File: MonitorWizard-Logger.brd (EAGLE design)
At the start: 84.4 x 80 mm, 40 parts, among them CON1 MICROSD, IC1 LD117AV33, J1 22-27-2041-04, J2 22-27-2041-04, J3 22-27-2041-04, U1 DHT22, U2 RFM69HW, U3 LTC3531, U4-NRF24L01 NRF24L01+-PCB-AERIAL, U6 ATMEGA328P-PU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

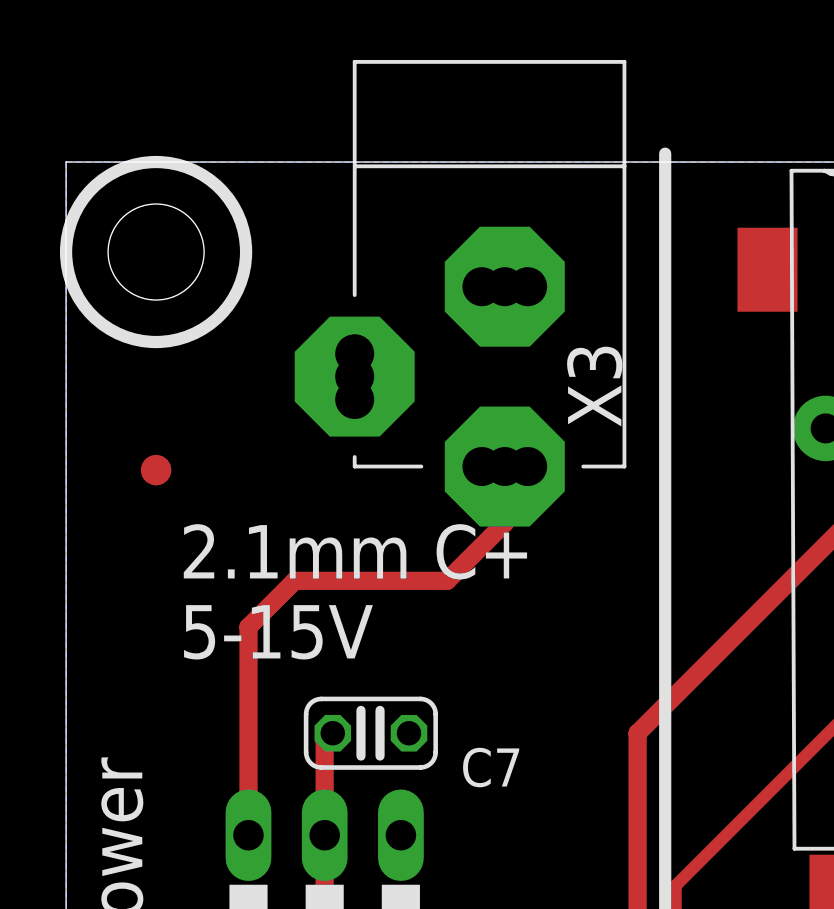
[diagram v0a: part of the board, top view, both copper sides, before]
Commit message: Change to a better barrel jack footprint
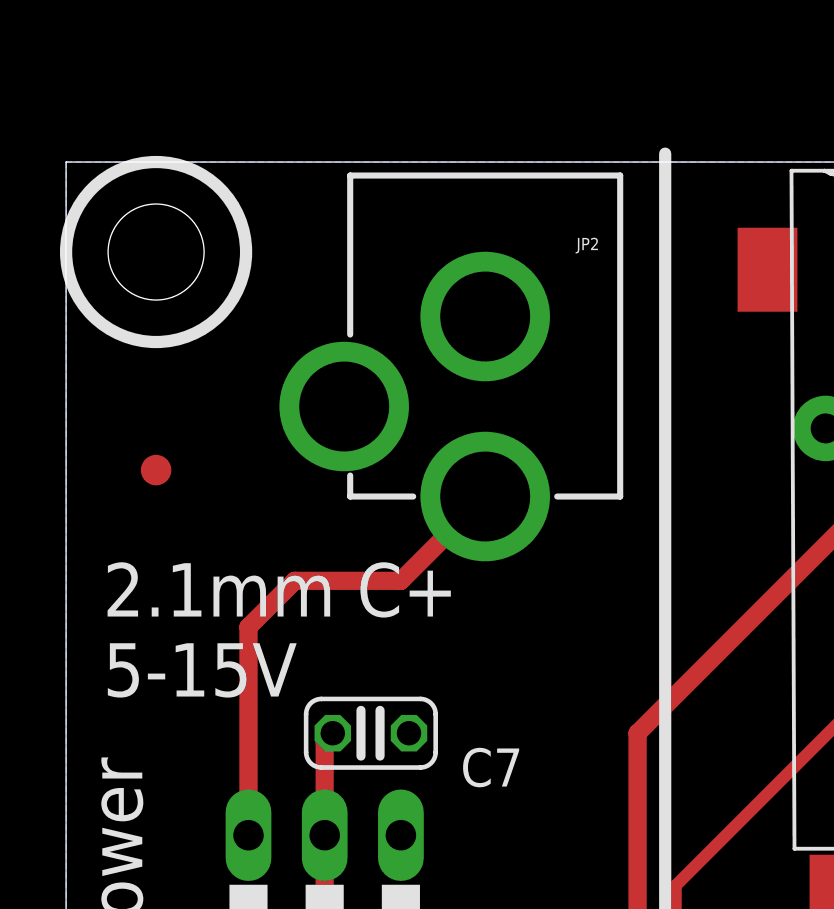
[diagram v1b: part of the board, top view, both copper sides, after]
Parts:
- removed X3: POWERSUPPLY_DC21MMX, SmartPrj:POWERSUPPLY_DC-21MM
- added JP2: POWER_JACKPTH, SparkFun-Connectors:POWER_JACK_PTH
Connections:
- net GND: now also JP2.GND, JP2.GNDBREAK; no longer X3.1, X3.3
- net VBJ: now also JP2.PWR; no longer X3.2
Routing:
- net VBJ: track 18.8 -> 16.6 mm
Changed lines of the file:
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@@
 <text x="33.94" y="2.54" size="1.778" layer="21" font="vector">MonitorWizard Development Board V1</text>
 <text x="32.67" y="36.83" size="1.778" layer="21" font="vector">Sensing</text>
-<text x="15.1925" y="63.4525" size="1.778" layer="21" font="vector">2.1mm C+
+<text x="12.6525" y="62.1825" size="1.778" layer="21" font="vector">2.1mm C+
 5-15V</text>
 <text x="66.23" y="76.2" size="1.778" layer="21" font="vector">Wireless</text>
@@
 </element>
 <element name="GND" library="Probes" package="ALLIGATOR" value="ALLIGATOR" x="22.94" y="0"/>
-<element name="X3" library="SmartPrj" package="POWERSUPPLY_DC-21MM" value="POWERSUPPLY_DC21MMX" x="26.13" y="76.2" smashed="yes">
-<attribute name="NAME" x="29.94" y="71.12" size="1.778" layer="25" ratio="5" rot="R90"/>
-</element>
 <element name="FD4" library="SmartPrj" package="FIDUCIA-MOUNT" value="FIDUCIALMOUNT" x="92.79" y="10.27"/>
 <element name="I_SENSE" library="Probes" package="CURRENT_MEASURE" value="CURRENT_MEASURE_0.4A" x="29.16" y="11.25" smashed="yes" rot="R180">
@@
 </element>
 <element name="C8" library="rcl" package="E2,5-6" value="" x="23.8125" y="34.6075" rot="R180"/>
+<element name="JP2" library="SparkFun-Connectors" package="POWER_JACK_PTH" value="POWER_JACKPTH" x="25.4" y="82.55" rot="R180">
+<attribute name="PROD_ID" value="CONN-08197" x="25.4" y="82.55" size="1.778" layer="27" rot="R180" display="off"/>
+</element>
 </elements>
 <signals>
@@
 <contactref element="GND" pad="TOP"/>
 <contactref element="GND" pad="BTM"/>
-<contactref element="X3" pad="3"/>
-<contactref element="X3" pad="1"/>
 <contactref element="U4-NRF24L01" pad="P$1"/>
 <contactref element="U6" pad="8"/>
@@
 <wire x1="22.94" y1="3.4925" x2="23.82" y2="3.5" width="0.6096" layer="16"/>
 <wire x1="23.82" y1="3.5" x2="22.94" y2="3.5" width="0.6096" layer="16"/>
+<contactref element="JP2" pad="GNDBREAK"/>
+<contactref element="JP2" pad="GND"/>
 </signal>
 <signal name="AREF" class="4">
@@
 </signal>
 <signal name="VBJ">
-<contactref element="X3" pad="2"/>
 <contactref element="IC1" pad="3"/>
 <wire x1="17.51" y1="57.56" x2="17.51" y2="64.5" width="0.6096" layer="1"/>
 <wire x1="17.51" y1="64.5" x2="19.05" y2="66.04" width="0.6096" layer="1"/>
-<wire x1="19.05" y1="66.04" x2="24.13" y2="66.04" width="0.6096" layer="1"/>
-<wire x1="24.13" y1="66.04" x2="26.0538" y2="67.9638" width="0.6096" layer="1"/>
-<wire x1="26.0538" y1="67.9638" x2="26.0538" y2="69.85" width="0.6096" layer="1"/>
+<contactref element="JP2" pad="PWR"/>
+<wire x1="19.05" y1="66.04" x2="22.59" y2="66.04" width="0.6096" layer="1"/>
+<wire x1="22.59" y1="66.04" x2="25.4" y2="68.85" width="0.6096" layer="1"/>
 </signal>
 <signal name="DHT22_DATA">

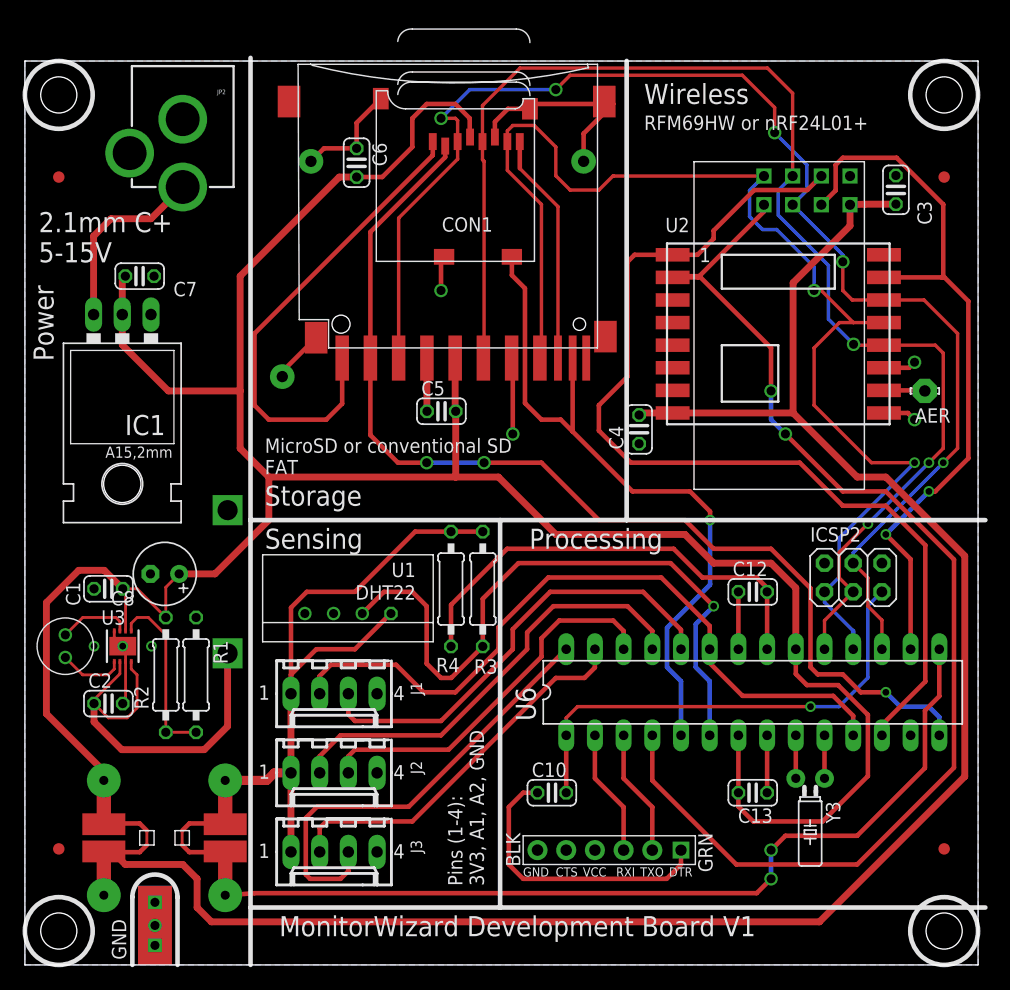
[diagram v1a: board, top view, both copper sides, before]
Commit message: Change footprint for LTC3531
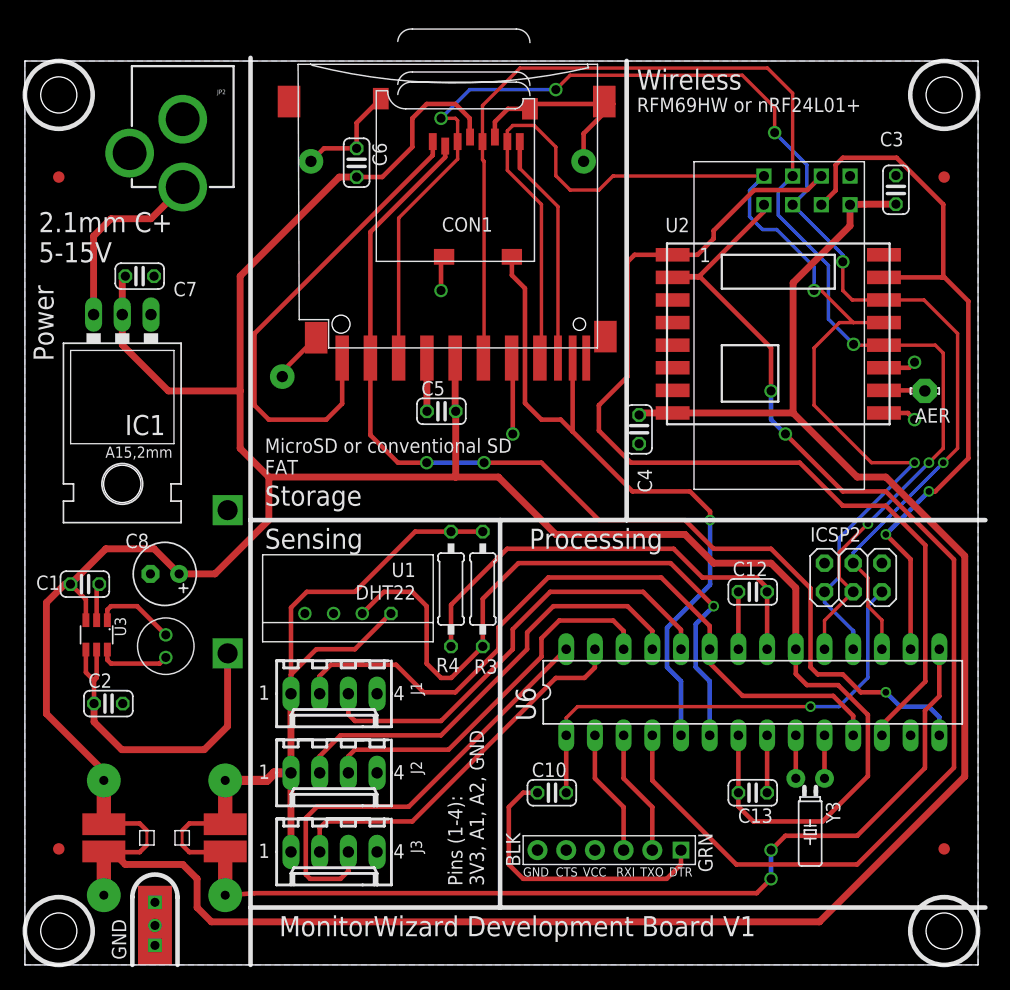
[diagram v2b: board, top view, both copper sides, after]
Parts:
- removed R1, R2: (no value), resistor:0207/10
- U3: device exported-lbrlinear-sen:DFN8-3X3 -> custom:TSOT23-6
- moved L1 8.89 mm to (23.9, 28.2)
- moved U3 2.52 mm to (17.8, 29.2), turned to 180 degrees
- moved C1 2.12 mm to (16.7, 33.7), turned to 0 degrees
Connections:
- removed net N$3: R1.2, R2.1, U3.5
- net 3V3: now also U3.3; no longer R2.2, U3.6
- net GND: now also U3.2; no longer R1.1, U3.3, U3.8, U3.EXP
- net N$1: now also U3.1; no longer U3.7
- net N$2: now also U3.6; no longer U3.1
- net VBAT: now also U3.5; no longer U3.2
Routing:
- net N$3: track 15.9 -> 0.00 mm
- net VBAT: track 35.6 -> 29.7 mm
- net GND: track 74.3 -> 70.5 mm, vias 11 -> 8
- net 3V3: track 222.7 -> 219.6 mm
- net N$1: track 6.45 -> 7.27 mm
- net N$2: track 5.85 -> 6.45 mm

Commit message: Move some stuff around, add a filter capacitor. As ordered from Screenbond
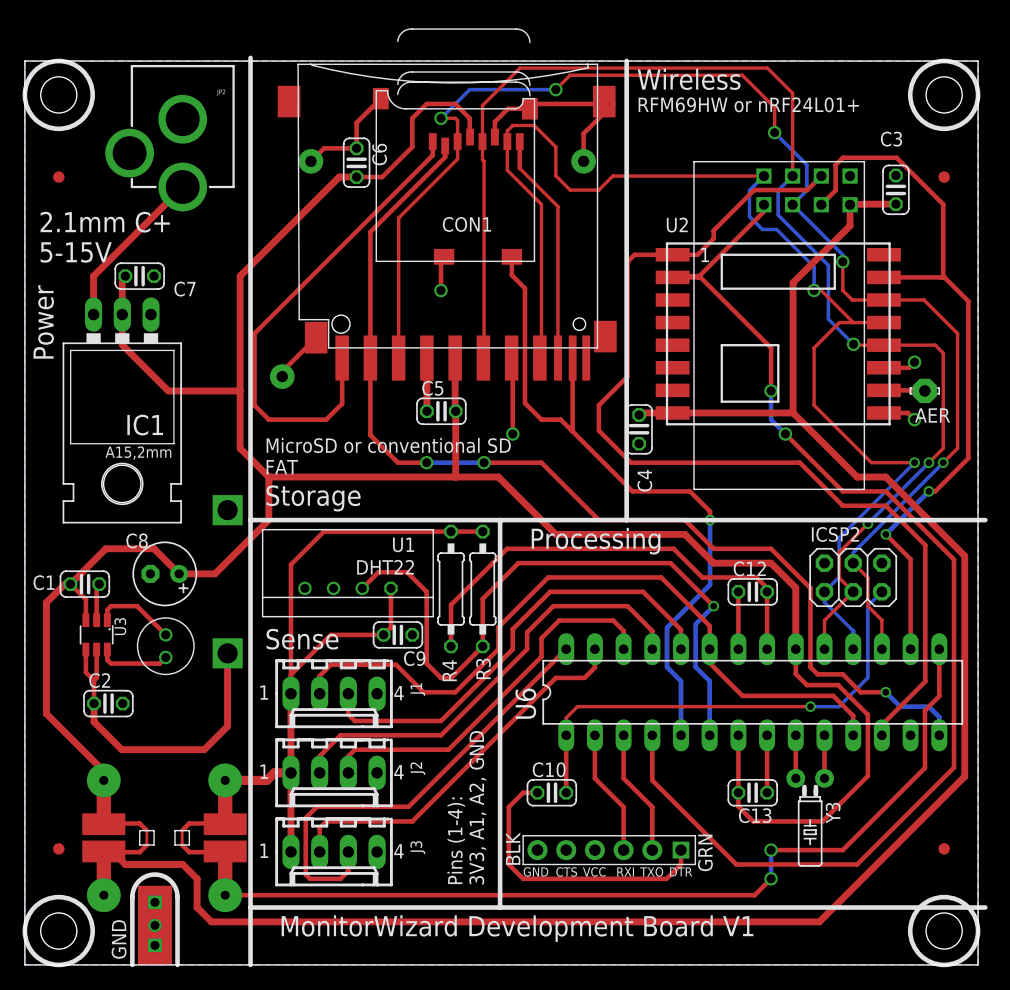
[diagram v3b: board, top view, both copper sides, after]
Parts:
- added C9: 0.1u, rcl:C025-024X044
- moved U1 2.22 mm to (40.0, 33.3)
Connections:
- net GND: now also C9.1
- net SENSOR_3V3: now also C9.2
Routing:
- net SENSOR_3V3: track 60.3 -> 65.4 mm
- net VBJ: track 16.6 -> 14.6 mm
- net DHT22_DATA: track 58.9 -> 60.1 mm
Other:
- board text added: "Sense"
- board text removed: "Sensing"
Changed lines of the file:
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@@
 <wire x1="11.43" y1="80" x2="11.43" y2="0" width="0" layer="20"/>
 <text x="33.94" y="2.54" size="1.778" layer="21" font="vector">MonitorWizard Development Board V1</text>
-<text x="32.67" y="36.83" size="1.778" layer="21" font="vector">Sensing</text>
+<text x="32.67" y="27.94" size="1.778" layer="21" font="vector">Sense</text>
 <text x="12.6525" y="62.1825" size="1.778" layer="21" font="vector">2.1mm C+
 5-15V</text>
@@
 <attribute name="NAME" x="26.085" y="12.795" size="0.8128" layer="27" rot="R90"/>
 </element>
-<element name="U1" library="RHT03_DHT-22_AM2302" package="RHT03_DHT-22" value="DHT22" x="40.02" y="31.1" rot="R180">
-<attribute name="PROD_ID" value="SEN-10167" x="40.02" y="31.1" size="1.778" layer="27" rot="R180" display="off"/>
+<element name="U1" library="RHT03_DHT-22_AM2302" package="RHT03_DHT-22" value="DHT22" x="40.02" y="33.3225" rot="R180">
+<attribute name="PROD_ID" value="SEN-10167" x="40.02" y="33.3225" size="1.778" layer="27" rot="R180" display="off"/>
 </element>
 <element name="R3" library="resistor" package="0207/10" value="10K" x="51.955" y="33.27" smashed="yes" rot="R90">
-<attribute name="NAME" x="51.177" y="25.769" size="1.27" layer="25" ratio="10"/>
+<attribute name="NAME" x="52.6535" y="25.142" size="1.27" layer="25" ratio="10" rot="R90"/>
 <attribute name="VALUE" x="51.2325" y="35.6656" size="1.27" layer="27" ratio="10" rot="R270"/>
 </element>
@@
 <element name="L1" library="InductorsThru" package="L-RADIAL-2-5OD" value="10uH" x="23.9" y="28.21" smashed="yes" rot="R90"/>
 <element name="C1" library="rcl" package="C025-024X044" value="10uH" x="16.74" y="33.7025" smashed="yes">
-<attribute name="NAME" x="12.422" y="33.1945" size="1.27" layer="25" ratio="10"/>
-<attribute name="VALUE" x="13.057" y="35.163" size="1.27" layer="27" ratio="10"/>
+<attribute name="NAME" x="12.1045" y="33.1945" size="1.27" layer="25" ratio="10"/>
+<attribute name="VALUE" x="12.1045" y="35.163" size="1.27" layer="27" ratio="10"/>
 </element>
 <element name="C2" library="rcl" package="C025-024X044" value="2.2uH" x="18.82" y="23.13"/>
@@
 </element>
 <element name="R4" library="resistor" package="0207/10" value="TBD" x="49.145" y="33.27" smashed="yes" rot="R270">
-<attribute name="NAME" x="47.8195" y="25.904" size="1.27" layer="25" ratio="10"/>
+<attribute name="NAME" x="49.661" y="24.9595" size="1.27" layer="25" ratio="10" rot="R90"/>
 <attribute name="VALUE" x="48.51" y="35.5306" size="1.27" layer="27" ratio="10" rot="R270"/>
 </element>
@@
 <attribute name="VALUE" x="14.9225" y="30.7975" size="1.016" layer="27" ratio="10" rot="R270"/>
 <attribute name="NAME" x="19.3675" y="30.7975" size="1.016" layer="25" ratio="10" rot="R270"/>
+</element>
+<element name="C9" library="rcl" package="C025-024X044" value="0.1u" x="44.45" y="29.21" smashed="yes" rot="R180">
+<attribute name="NAME" x="44.8945" y="26.4795" size="1.27" layer="25" ratio="10"/>
 </element>
 </elements>
@@
 <contactref element="C2" pad="2"/>
 <contactref element="C1" pad="2"/>
-<wire x1="20.34" y1="23.13" x2="20.09" y2="23.13" width="0" layer="19" extent="1-16"/>
 <contactref element="IC1" pad="1"/>
 <wire x1="77.12" y1="15.24" x2="77.12" y2="20.32" width="0.4064" layer="1"/>
@@
 <wire x1="17.78" y1="33.4725" x2="17.78" y2="30.51" width="0.4064" layer="1"/>
 <wire x1="17.78" y1="33.4725" x2="18.01" y2="33.7025" width="0.4064" layer="1"/>
+<contactref element="C9" pad="1"/>
 </signal>
 <signal name="AREF" class="4">
@@
 <signal name="VBJ">
 <contactref element="IC1" pad="3"/>
-<wire x1="17.51" y1="57.56" x2="17.51" y2="64.5" width="0.6096" layer="1"/>
-<wire x1="17.51" y1="64.5" x2="19.05" y2="66.04" width="0.6096" layer="1"/>
+<wire x1="17.51" y1="57.56" x2="17.51" y2="60.96" width="0.6096" layer="1"/>
+<wire x1="17.51" y1="60.96" x2="22.59" y2="66.04" width="0.6096" layer="1"/>
 <contactref element="JP2" pad="PWR"/>
-<wire x1="19.05" y1="66.04" x2="22.59" y2="66.04" width="0.6096" layer="1"/>
 <wire x1="22.59" y1="66.04" x2="25.4" y2="68.85" width="0.6096" layer="1"/>
 </signal>
@@
 <wire x1="55.11" y1="35.56" x2="51.955" y2="32.405" width="0.4064" layer="1"/>
 <wire x1="51.955" y1="32.405" x2="51.955" y2="28.19" width="0.4064" layer="1"/>
-<wire x1="41.29" y1="31.1" x2="43.21" y2="33.02" width="0.4064" layer="1"/>
-<wire x1="43.21" y1="33.02" x2="45.72" y2="33.02" width="0.4064" layer="1"/>
-<wire x1="45.72" y1="33.02" x2="46.99" y2="31.75" width="0.4064" layer="1"/>
-<wire x1="46.99" y1="31.75" x2="46.99" y2="26.67" width="0.4064" layer="1"/>
+<wire x1="41.29" y1="33.3225" x2="42.72186875" y2="34.75436875" width="0.4064" layer="1"/>
+<wire x1="42.72186875" y1="34.75436875" x2="45.25563125" y2="34.75436875" width="0.4064" layer="1"/>
+<wire x1="45.25563125" y1="34.75436875" x2="46.99" y2="33.02" width="0.4064" layer="1"/>
+<wire x1="46.99" y1="33.02" x2="46.99" y2="26.67" width="0.4064" layer="1"/>
 <wire x1="46.99" y1="26.67" x2="48.26" y2="25.4" width="0.4064" layer="1"/>
 <wire x1="48.26" y1="25.4" x2="49.165" y2="25.4" width="0.4064" layer="1"/>
@@
 <wire x1="20.32" y1="60.96" x2="20.05" y2="60.69" width="0.6096" layer="1"/>
 <wire x1="20.05" y1="60.69" x2="20.05" y2="57.56" width="0.6096" layer="1"/>
-<wire x1="23.9" y1="33.425" x2="25.0825" y2="34.6075" width="0" layer="19" extent="1-16"/>
 <wire x1="25.0825" y1="34.6075" x2="28.2575" y2="34.6075" width="0.6096" layer="1"/>
 <wire x1="28.2575" y1="34.6075" x2="33.02" y2="39.37" width="0.6096" layer="1"/>
@@
 <wire x1="92.36" y1="23.78" x2="91.09" y2="22.51" width="0.4064" layer="1"/>
 <wire x1="91.09" y1="22.51" x2="91.09" y2="17.43" width="0.4064" layer="1"/>
-<wire x1="91.09" y1="17.43" x2="85.09" y2="11.43" width="0.4064" layer="1"/>
-<wire x1="85.09" y1="11.43" x2="78.74" y2="11.43" width="0.4064" layer="1"/>
-<wire x1="78.74" y1="11.43" x2="77.47" y2="10.16" width="0.4064" layer="1"/>
-<via x="77.47" y="10.16" extent="1-16" drill="0.8" shape="square"/>
+<wire x1="91.09" y1="17.43" x2="83.82" y2="10.16" width="0.4064" layer="1"/>
+<via x="77.47" y="10.16" extent="1-16" drill="0.8"/>
 <wire x1="77.47" y1="10.16" x2="77.47" y2="7.62" width="0.4064" layer="16"/>
-<via x="77.47" y="7.62" extent="1-16" drill="0.8" shape="square"/>
-<wire x1="77.47" y1="7.62" x2="76.2" y2="6.35" width="0.4064" layer="1"/>
-<wire x1="76.2" y1="6.35" x2="31.75" y2="6.35" width="0.4064" layer="1"/>
-<wire x1="31.75" y1="6.35" x2="29.39" y2="6.17" width="0.4064" layer="1"/>
-<wire x1="29.39" y1="6.17" x2="29.16" y2="6.17" width="0.4064" layer="1"/>
+<via x="77.47" y="7.62" extent="1-16" drill="0.8"/>
+<wire x1="77.47" y1="7.62" x2="76.02" y2="6.17" width="0.4064" layer="1"/>
+<wire x1="29.16" y1="6.17" x2="76.02" y2="6.17" width="0.4064" layer="1"/>
+<wire x1="77.47" y1="10.16" x2="83.82" y2="10.16" width="0.4064" layer="1"/>
 </signal>
 <signal name="N$1">
@@
 <contactref element="R4" pad="1"/>
 <wire x1="34.98" y1="24" x2="34.98" y2="17" width="0.6096" layer="1"/>
-<wire x1="43.83" y1="31.1" x2="43.8" y2="31.1" width="0.4064" layer="1"/>
-<wire x1="43.8" y1="31.1" x2="40.64" y2="27.94" width="0.4064" layer="1"/>
-<wire x1="40.64" y1="27.94" x2="37.22396875" y2="27.94" width="0.4064" layer="1"/>
-<wire x1="37.22396875" y1="27.94" x2="34.98" y2="25.69603125" width="0.4064" layer="1"/>
+<wire x1="38.49396875" y1="29.21" x2="34.98" y2="25.69603125" width="0.4064" layer="1"/>
 <wire x1="34.98" y1="25.69603125" x2="34.98" y2="24" width="0.4064" layer="1"/>
 <wire x1="34.98" y1="17" x2="34.98" y2="10" width="0.6096" layer="1"/>
 <wire x1="33.51" y1="17" x2="34.98" y2="17" width="0.8128" layer="1"/>
 <wire x1="51.955" y1="38.35" x2="49.145" y2="38.35" width="0.4064" layer="1"/>
-<wire x1="49.145" y1="38.35" x2="45.97" y2="38.35" width="0.4064" layer="1"/>
-<wire x1="45.97" y1="38.35" x2="40.64" y2="33.02" width="0.4064" layer="1"/>
-<wire x1="40.64" y1="33.02" x2="36.376171875" y2="33.02" width="0.4064" layer="1"/>
-<wire x1="36.376171875" y1="33.02" x2="34.98" y2="31.623828125" width="0.4064" layer="1"/>
-<wire x1="34.98" y1="31.623828125" x2="34.98" y2="24" width="0.4064" layer="1"/>
+<wire x1="49.145" y1="38.35" x2="37.896171875" y2="38.35" width="0.4064" layer="1"/>
+<wire x1="37.896171875" y1="38.35" x2="34.98" y2="35.433828125" width="0.4064" layer="1"/>
+<wire x1="34.98" y1="35.433828125" x2="34.98" y2="24" width="0.4064" layer="1"/>
 <wire x1="33.51" y1="17" x2="32.84" y2="16.33" width="0.8128" layer="1"/>
 <wire x1="32.84" y1="16.33" x2="29.16" y2="16.33" width="0.8128" layer="1"/>
+<contactref element="C9" pad="2"/>
+<wire x1="38.49396875" y1="29.21" x2="43.18" y2="29.21" width="0.4064" layer="1"/>
+<wire x1="43.18" y1="29.21" x2="43.83" y2="29.86" width="0.4064" layer="1"/>
+<wire x1="43.83" y1="29.86" x2="43.83" y2="33.3225" width="0.4064" layer="1"/>
 </signal>
 </signals>
